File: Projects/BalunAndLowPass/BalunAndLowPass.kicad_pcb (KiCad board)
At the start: 2 copper layers, 55.9 x 54.6 mm, 16 parts, among them J1 SMA-J-P-H-ST-EM1, J2 SMA-J-P-H-ST-EM1, J3 SMA-J-P-H-ST-EM1, J4 SMA-J-P-H-ST-EM1, J5 SMA-J-P-H-ST-EM1, J6 SMA-J-P-H-ST-EM1

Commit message: added full board
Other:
- board text added: "GTRF Single Ended Combiner"

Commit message: post board review they are all ready to order
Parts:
- added L11: 470nH, Inductor_SMD:L_0805_2012Metric, F.Cu at (93.6, 95.4)
- added L22: 470nH, Inductor_SMD:L_0805_2012Metric, F.Cu at (93.6, 69.9)
- moved L1 2.59 mm to (88.8, 95.4)
- moved L2 2.54 mm to (88.9, 70.0)
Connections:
- L1 pad 1: /I_Filtered -> Net-(L1-Pad1)
- L2 pad 1: /Q_Filtered -> Net-(L2-Pad1)
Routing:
- net /I_Single_Ended: track 9.48 -> 6.50 mm
- net /Q_Single_Ended: track 9.26 -> 6.75 mm
- net Net-(L1-Pad1): track 0.00 -> 2.44 mm
- net Net-(L2-Pad1): track 0.00 -> 2.39 mm
- net /Q_Filtered: track 13.4 -> 11.2 mm
- net /I_Filtered: track 12.9 -> 10.8 mm
- net GND: vias 393 -> 389

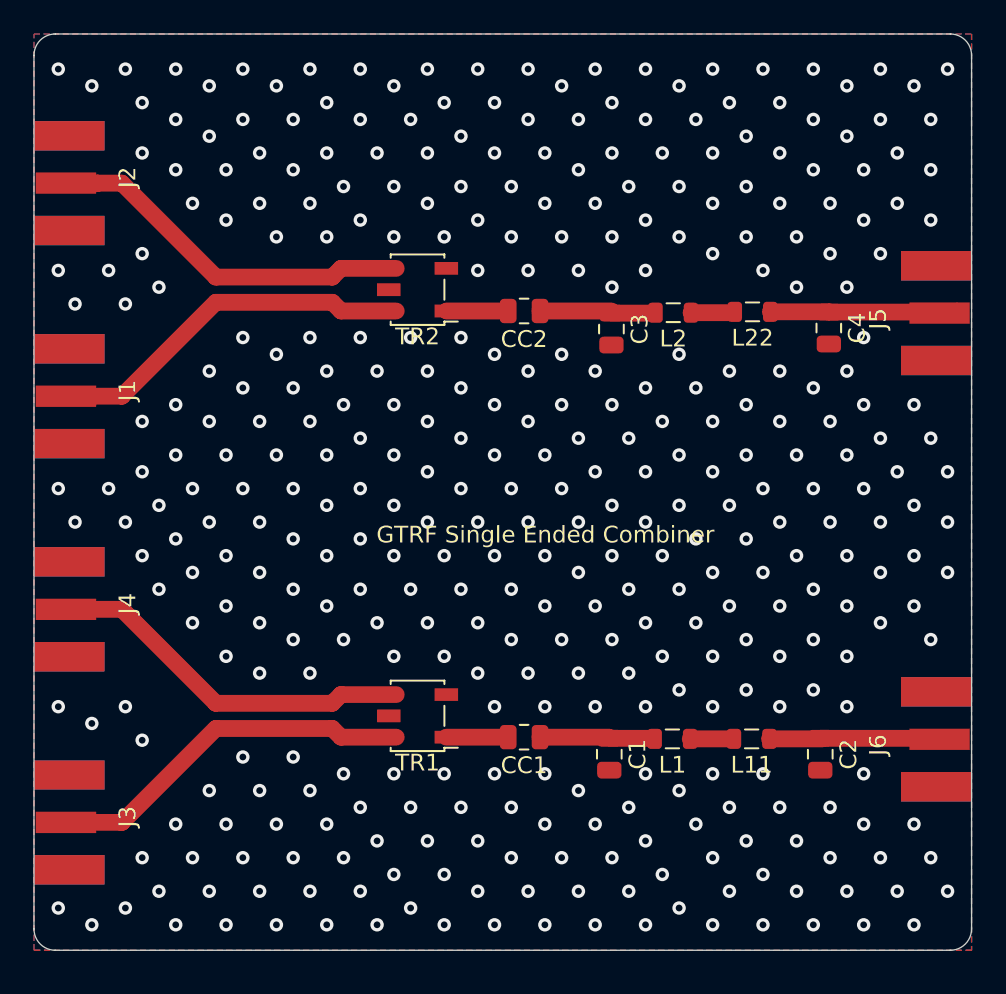
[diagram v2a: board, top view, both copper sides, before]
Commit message: Power Detector and power splitter boards designed
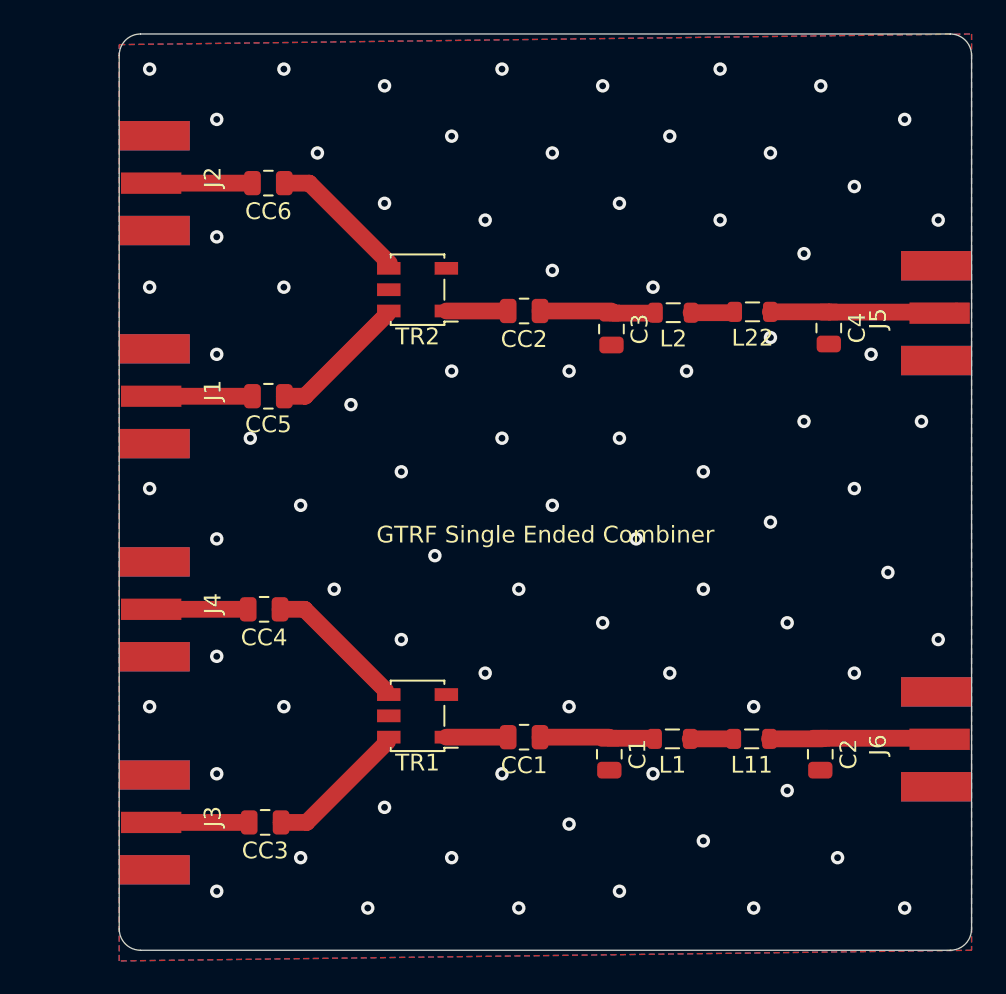
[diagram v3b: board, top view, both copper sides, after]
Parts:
- added CC3: .47uF, Capacitor_SMD:C_0805_2012Metric, F.Cu at (64.6, 100.3)
- added CC4: .47uF, Capacitor_SMD:C_0805_2012Metric, F.Cu at (64.5, 87.6)
- added CC5: .47uF, Capacitor_SMD:C_0805_2012Metric, F.Cu at (64.8, 74.9)
- added CC6: .47uF, Capacitor_SMD:C_0805_2012Metric, F.Cu at (64.8, 62.2)
- moved J1 5.08 mm to (57.8, 74.9)
- moved J2 5.08 mm to (57.8, 62.2)
- moved J3 5.08 mm to (57.8, 100.3)
- moved J4 5.08 mm to (57.8, 87.6)
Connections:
- J1 pad 1: /Q+ -> Net-(CC5-Pad2)
- J2 pad 1: /Q- -> Net-(CC6-Pad2)
- J3 pad 1: /I+ -> Net-(CC3-Pad2)
- J4 pad 1: /I- -> Net-(CC4-Pad2)
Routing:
- net /Q-: track 24.7 -> 8.24 mm
- net /I-: track 22.8 -> 8.29 mm
- net /I+: track 22.8 -> 8.35 mm
- net /Q+: track 22.2 -> 8.20 mm
- net Net-(CC5-Pad2): track 0.00 -> 5.97 mm
- net Net-(CC6-Pad2): track 0.00 -> 5.84 mm
- net Net-(CC4-Pad2): track 0.00 -> 5.72 mm
- net Net-(CC3-Pad2): track 0.00 -> 5.59 mm
- net GND: vias 389 -> 80
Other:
- board size 55.9 x 54.6 mm -> 50.8 x 54.6 mm
